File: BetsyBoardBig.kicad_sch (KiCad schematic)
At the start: 73 parts, among them J1 CLOCKS, J2 SPI, J3 USB_C_Receptacle_USB2.0, J5 I2C, J6 USART3, J7 ANALOG, J8 Micro_SD_Card, J9 USART1, P1 BATT, P2 CORTEX-JTAG, Q1 FDN340P, SW1 JUMPER, SW2 TE-FSM4J, SW3 SW_PUSH_NO_ALT, U1 TLV75733PDBVR‎, U2 USBLC6-2SC6, U3 74LVC3G14, U4 STM32L486Rx-LQFP64, U5 74LVC1G3157, U6 IS25LP06D-xB, U7 MCP73831-2-OT, X1 XTAL, Y1 Crystal

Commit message: More work on battery charging.
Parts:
- removed D3: B130LAW, Diode_SMD:D_SOD-123, symbol Device:D_Schottky
- removed D4: RED, LED_SMD:LED_0603_1608Metric, symbol Device:LED
- removed Q1: FDN340P, Package_TO_SOT_SMD:SOT-23, symbol Transistor_FET:FDN340P
- removed R4: 470, Resistor_SMD:R_0603_1608Metric, symbol Device:R_US
- removed TP3: TestPoint_Probe, engstad:pin-socket-1, symbol Connector:TestPoint_Probe
- removed U5: 74LVC1G3157, Package_TO_SOT_SMD:SOT-23-6, symbol 74xGxx:74LVC1G3157
- removed U7: MCP73831-2-OT, Package_TO_SOT_SMD:SOT-23-5, symbol Battery_Management:MCP73831-2-OT
- added C24, C25: 0.1uF, Capacitor_SMD:C_0603_1608Metric, symbol Device:C_Small
- added C7: 4.7uF, Capacitor_SMD:C_0805_2012Metric, symbol Device:C
- added D1: RED, LED_SMD:LED_0603_1608Metric, symbol Device:LED
- added P2: BATT, engstad:pin-socket-2, symbol Connector_Generic:Conn_01x02
- added R1: 330K, Resistor_SMD:R_0603_1608Metric, symbol Device:R_US
- added R12: 330, Resistor_SMD:R_0603_1608Metric, symbol Device:R_US
- added R2: 110K, Resistor_SMD:R_0603_1608Metric, symbol Device:R_US
- added TP2: TestPoint_Probe, TestPoint:TestPoint_Pad_1.0x1.0mm, symbol Connector:TestPoint_Probe
- added U3: MCP73871, Package_DFN_QFN:QFN-20-1EP_4x4mm_P0.5mm_EP2.5x2.5mm, symbol Battery_Management:MCP73871
- added U4: 74LVC1G08, Package_TO_SOT_SMD:SOT-23-5, symbol @Engstad:74LVC1G08
- added U7: 74LVC1G3157, Package_TO_SOT_SMD:SOT-23-6, symbol Engstad:74LVC1G3157
- B1: footprint engstad:Battery_Keystone_2894 -> Engstad:Battery_Keystone_2894
- C1: renamed from C21; value 1uF -> 10uF
- C4: renamed from C22; value 1uF -> 4.7uF
- J8: footprint SDMMC -> Engstad:Molex_PS_105162_001
- R14: renamed from R7; value 1K -> 330
- R5: renamed from R11; value 100K -> 10K
- R6: renamed from R10; value 1K -> 100K
- SW2, SW3: footprint engstad:TACTILE_SWITCH-TE-FSM4JSMAATR -> Engstad:TACTILE_SWITCH-TE-FSM4JSMAATR
- U5: renamed from U3; symbol 74xGxx:74LVC3G14 -> Engstad:74LVC3G14
- U6: renamed from U4; symbol @Engstad:STM32L486Rx-LQFP64 -> Engstad:STM32L486Rx-LQFP64
- renumbered C11 to C10, C12 to C11, C7 to C12, C8 to C13, C9 to C14, C10 to C15, C13 to C16, C15 to C17, C16 to C18, C17 to C19, C5 to C2, C18 to C20, C19 to C21, C14 to C22, C20 to C23, C6 to C3, C3 to C5, C4 to C6, C2 to C8, C1 to C9, D1 to D2, D2 to D3, FB2 to FB1, J3 to J1, J1 to J2, J2 to J3, J5 to J4, J6 to J5, J7 to J6, J9 to J7, P2 to P3, R5 to R10, R12 to R11, R6 to R13, R8 to R3, R9 to R4, R1 to R7, R2 to R8, R3 to R9, TP2 to TP3, U6 to U8
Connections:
- net GND: now also C24.2, C25.2, C7.2, P2.2 (Pin_2), R2.1, U3.10 (V_{SS}), U3.11 (V_{SS}), U3.21 (V_{SS}), U3.3 (SEL), U3.4 (PROG2), U3.9 (~{TE}), U4.3 (GND), U7.2 (GND)
- net PB13: now also U7.4
- net SEL_USART3: now also U7.6
- net SPI2_SCK: now also U7.3
- net USART3_CTS: now also U7.1
- net VBUS: now also D1.2 (A), R1.2, U3.17 (CE), U3.18 (IN), U3.19 (IN); no longer R5.2
- net VCC: now also C24.1, C25.1, U4.5 (VCC), U7.5 (VCC)
- net VIN: now also C4.1, U3.1 (OUT), U3.20 (OUT)
- net ~{JTRST}: now also U4.1
- net ~{MR}: now also U5.6; no longer U5.3
- net ~{RST}: now also U4.4; no longer U5.2
- net SW: now reaches R7.2, R8.2, SW2.2
- net BOOT_{M}: now reaches U5.7
- net BOOT_{M}: now also R9.2; no longer U5.6
- net ~{RST_{M}}: now reaches U5.5
- net ~{RST_{M}}: now also TP2.1, U4.2; no longer R9.2
- net PB8: no longer names the net of U6.61 (PB8/I2C1_SCL/SDD4)
- net PRG renamed PRG3
- net PRG3: now also U3.12 (PROG3)
- net SPI2_CIPO renamed SPI2_POCI
- net SPI2_COPI renamed SPI2_PICO
- net VBATT renamed V_BAT
- net V_BAT: now also C7.1, U3.14 (V_{BAT}), U3.15 (V_{BAT}), U3.16 (V_{BAT_SENSE}); no longer C4.1
- new net: D1.1 (K), R12.1
- new net PRG1: R5.2, U3.13 (PROG1)
- new net RST_{M}: U5.2, U5.3
- new net THM: P2.1 (Pin_1), U3.5 (THERM)
- new net VPCC: R1.1, R2.2, U3.2 (VPCC)
- new net ~{PG}: R12.2, U3.6 (~{PG})
- no-connect marks 4 -> 7
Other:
- note added: "5.5V/20mA = 275 ohm 3.3V/20mA = 165 ohm (1%) 160 (5%) or 180 (10%)"
- note added: "RST = BTN | TRST => ~{RST} = ~{BTN} & ~{TRST} ~{BTN} ~{TRST} ~{RST} 0 0 0 0 1 0 1 0 0 1 1 1"
- note added: "SEL : 0 = USB-port, 1 = AC-DC adapter (high current). PROG2: 0 = USB-port current limit (0 = 100mA, 1 = 500mA). ~{TE} : 0 = Enable safety timer. PROG3: Termination set-point. (10K = 100mA, 100K = 10mA). PROG1: Fast-charge current regulation:. (1K = 1000 mA, 10K = 100 mA). CE : Device charge enable. VPCC : Disabled if connected to V_{IN}."
- note added: "THM uses a 10K thermistor."
- note added: "V_{VPCC} = R_{2} / (R_{1} + R_{2}) * V_{i} = 1.23 V"
- note removed: "3.3V/20mA = 165 ohm (1%) 160 (5%) or 180 (10%)"
- note removed: "D"
- note removed: "G"
- note removed: "In order for switch to turn on, VIN = Vs >= Vg + Vth = VBUS + Vth. With battery powered, the body diode makes Vs = 4.2V - 0.7V = 3.5V, for a moment. Then 3.5V >= 0V + 2V, so the switch turns on, bringing VIN to 4.2V - Rds * Id. When VBATT is 0V, and VBUS = 5V, then VIN = 5V - 0..3V = 4.7V < VBUS.+ Vth = 5V + 2V = 7V, so the switch is off, and VIN = VBUS - 0.3V"
- note removed: "S"
- moved on the sheet: B1, C1, C10, C11, C12, C13, C14, C15, C16, C17, C18, C19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

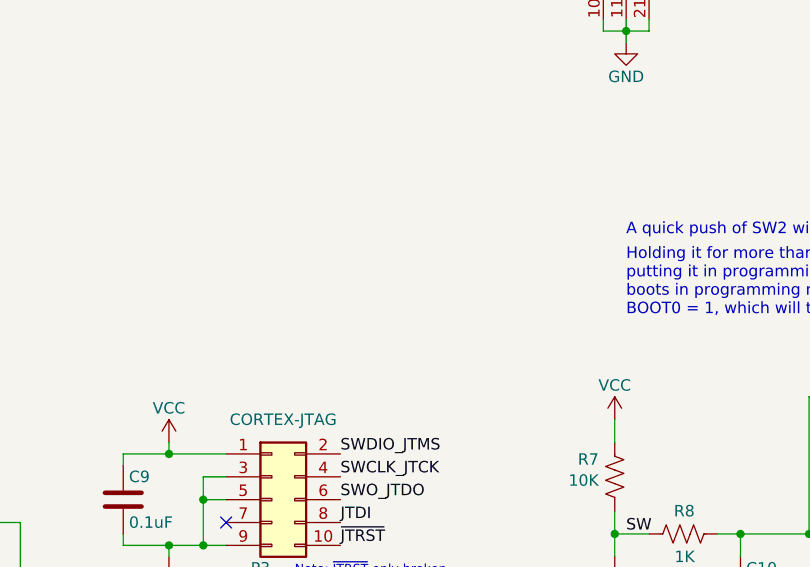
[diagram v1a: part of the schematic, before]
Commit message: Reworking reset pin on JTAG/SWD header and adding AND-gate.
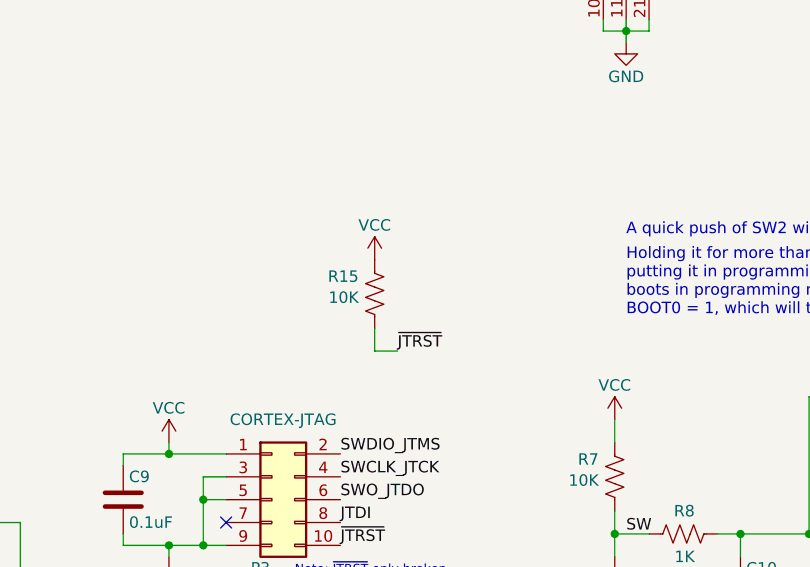
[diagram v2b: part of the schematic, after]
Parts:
- added R15: 10K, Resistor_SMD:R_0603_1608Metric, symbol Device:R_US
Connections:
- net VCC: now also R15.1
- net ~{JTRST}: now also R15.2
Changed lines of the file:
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@@
     (stroke (width 0) (type default))
   )
+  (wire (pts (xy 142.24 115.57) (xy 139.7 115.57))
+    (stroke (width 0) (type default))
+  )
   (wire (pts (xy 198.12 269.24) (xy 198.12 271.78))
     (stroke (width 0) (type default))
@@
     (stroke (width 0) (type default))
   )
+  (wire (pts (xy 139.7 115.57) (xy 139.7 113.03))
+    (stroke (width 0) (type default))
+  )
   (wire (pts (xy 48.26 41.91) (xy 48.26 43.18))
     (stroke (width 0) (type default))
@@
     (effects (font (size 1.27 1.27)) (justify right bottom))
   )
+  (label "~{JTRST}" (at 142.24 115.57 0) (fields_autoplaced)
+    (effects (font (size 1.27 1.27)) (justify left bottom))
+  )
   (label "USART1_RX" (at 344.17 132.08 0) (fields_autoplaced)
     (effects (font (size 1.27 1.27)) (justify left bottom))
@@
     )
   )
+  (symbol (lib_id "power:VCC") (at 139.7 105.41 0) (unit 1)
+    (in_bom yes) (on_board yes) (dnp no)
+    (property "Reference" "#PWR0100" (at 139.7 109.22 0)
+      (effects (font (size 1.27 1.27)) hide)
+    )
+    (property "Value" "VCC" (at 139.7 101.6 0)
+      (effects (font (size 1.27 1.27)))
+    )
+    (property "Footprint" "" (at 139.7 105.41 0)
+      (effects (font (size 1.27 1.27)) hide)
+    )
+    (property "Datasheet" "" (at 139.7 105.41 0)
+      (effects (font (size 1.27 1.27)) hide)
+    )
+    (pin "1")
+    (instances
+      (project "BetsyBoardBig"
+        (path "/91c25104-85f0-46da-beb1-0a469577067a"
+          (reference "#PWR0100") (unit 1)
+        )
+      )
+    )
+  )
   (symbol (lib_id "power:VBUS") (at 185.42 246.38 0) (unit 1)
     (in_bom yes) (on_board yes) (dnp no) (fields_autoplaced)
@@
         )
       )
+    )
+  )
+  (symbol (lib_id "Device:R_US") (at 139.7 109.22 0) (unit 1)
+    (in_bom yes) (on_board yes) (dnp no)
+    (property "Reference" "R15" (at 137.922 107.2896 0)
+      (effects (font (size 1.27 1.27)) (justify right))
+    )
+    (property "Value" "10K" (at 137.922 109.6264 0)
+      (effects (font (size 1.27 1.27)) (justify right))
+    )
+    (property "Footprint" "Resistor_SMD:R_0603_1608Metric" (at 137.922 111.5568 0)
+      (effects (font (size 0.762 0.762)) (justify right) hide)
+    )
+    (property "Datasheet" "" (at 139.7 109.22 0)
+      (effects (font (size 0.762 0.762)))
+    )
+    (pin "1")
+    (pin "2")
+    (instances
+      (project "BetsyBoardBig"
+        (path "/91c25104-85f0-46da-beb1-0a469577067a"
+          (reference "R15") (unit 1)
+        )
+      )
